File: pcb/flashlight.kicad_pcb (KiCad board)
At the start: 2 copper layers, 15.8 x 15.8 mm, 29 parts, among them IC1 TPS61200, IC2 PIC10F320

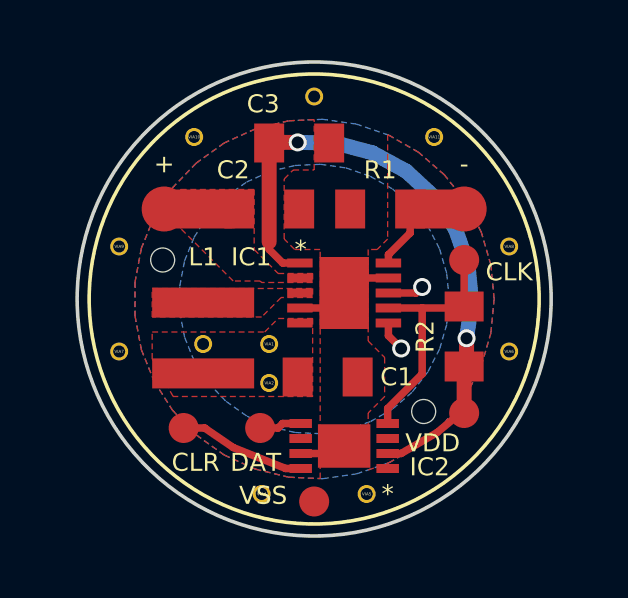
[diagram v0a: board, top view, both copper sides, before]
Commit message: move programming pads to bottom and add support extensions
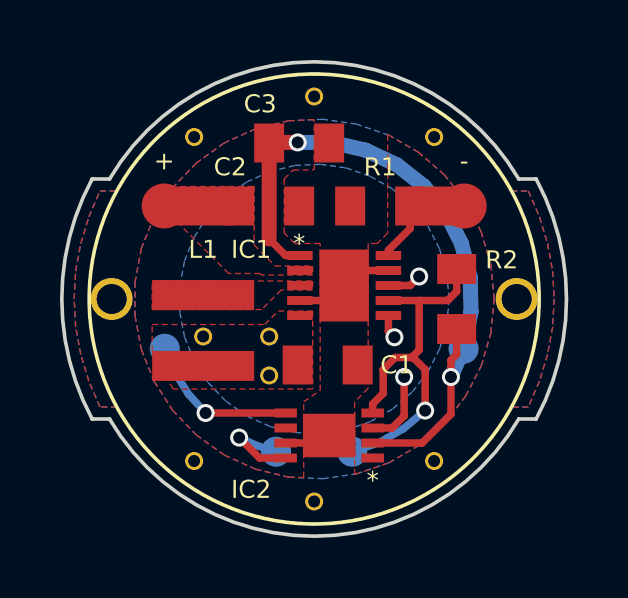
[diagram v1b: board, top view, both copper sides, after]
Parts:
- removed ? (x2): DRILL-0.8mm, modules:DRILL-0.8mm
- removed the VIA6 at (156.5, 101.8)
- removed the VIA7 at (143.5, 101.8)
- removed the VIA8 at (156.5, 98.2)
- removed VSS: VSS, modules:PAD-1.0mm
- added PIN1: PIN, modules:PIN-1.0mm, F.Cu at (143.2, 100.0)
- added PIN2: PIN, modules:PIN-1.0mm, F.Cu at (156.8, 100.0)
- MCLR: renamed from CLR; moved to B.Cu
- PCLK: renamed from CLK; moved to B.Cu
- PDAT: renamed from DAT; moved to B.Cu
- VDD: moved to B.Cu
- moved VIA6 13.4 mm to (154.0, 105.4)
- moved VIA9 11.1 mm to (154.0, 94.6)
- moved VIA7 8.00 mm to (146.0, 94.6)
- moved PCLK 7.40 mm to (151.3, 105.1)
- moved PDAT 4.13 mm to (145.0, 101.7)
- moved MCLR 3.18 mm to (148.7, 105.1)
- moved VIA4 2.50 mm to (146.0, 105.4)
- moved VDD 2.14 mm to (155.0, 101.7)
- moved VIA5 1.77 mm to (150.0, 106.8)
- moved R2 1.27 mm to (154.8, 100.0)
- moved IC2 0.61 mm to (150.5, 104.5)
- moved C1 0.40 mm to (150.4, 102.2)
- moved IC1 0.25 mm to (151.0, 99.5)
- moved L1 0.25 mm to (146.3, 101.0)
- moved VIA1 0.25 mm to (148.5, 101.2)
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- renumbered VIA10 to VIA6, VIA11 to VIA7, VIA12 to VIA8
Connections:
- IC2 pad 1: GND -> (no net)
- IC2 pad 3: (no net) -> SUPPLY
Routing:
- net N$4: track 8.45 -> 12.7 mm, vias 0 -> 1
- net N$6: track 1.41 -> 5.23 mm, vias 0 -> 1
- net SUPPLY: track 2.23 -> 4.47 mm, vias 2 -> 3
- net GND: track 4.92 -> 7.04 mm
- net N$3: track 21.2 -> 22.8 mm
- net N$7: track 4.24 -> 3.15 mm, vias 0 -> 1
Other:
- board size 15.8 x 15.8 mm -> 16.8 x 15.8 mm

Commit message: reduce radius of supply mask and move supply vias
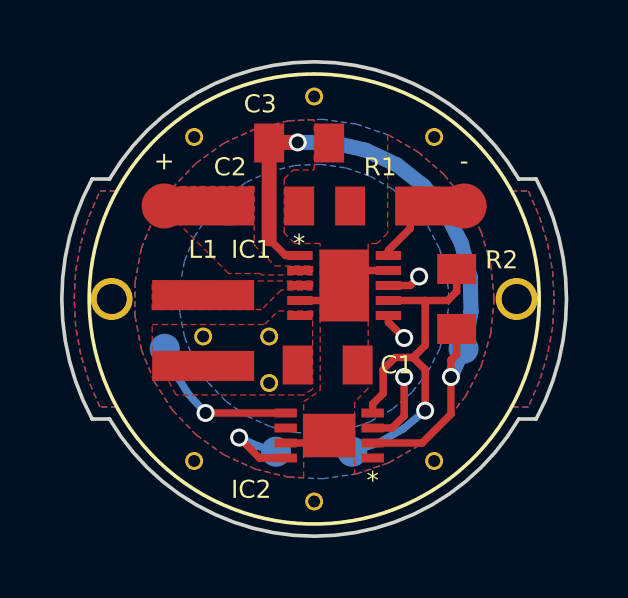
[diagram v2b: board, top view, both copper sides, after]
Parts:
- moved VIA2 0.25 mm to (148.5, 102.8)
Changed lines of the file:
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@@
     (thickness 1.6)
     (drawings 11)
-    (tracks 76)
+    (tracks 77)
     (zones 0)
     (modules 25)
@@
     (36 B.SilkS user)
     (37 F.SilkS user)
-    (38 B.Mask user hide)
+    (38 B.Mask user)
     (39 F.Mask user)
     (40 Dwgs.User user)
@@
   )
   (module modules:VIA-0.6mm (layer F.Cu)
-    (at 148.5 102.55)
+    (at 148.5 102.8)
     (fp_text reference VIA2 (at 0 0) (layer F.SilkS) hide
       (effects (font (size 0.2 0.2) (thickness 0.01)))
@@
   )
   (gr_circle (center 150 100) (end 157.5 100) (layer F.SilkS) (width 0.12))
-  (segment (start 152.475 100.55) (end 152.475 101.075) (width 0.25) (layer F.Cu) (net 1))
-  (segment (start 152.475 101.075) (end 152.675 101.275) (width 0.25) (layer F.Cu) (net 1))
-  (via (at 152.675 101.275) (size 0.6) (drill 0.4) (layers F.Cu B.Cu) (net 1))
+  (segment (start 152.475 100.55) (end 152.475 100.775) (width 0.25) (layer F.Cu) (net 1))
+  (via (at 153 101.3) (size 0.6) (drill 0.4) (layers F.Cu B.Cu) (net 1))
+  (segment (start 152.475 100.775) (end 153 101.3) (width 0.25) (layer F.Cu) (net 1))
   (segment (start 152.475 99.55) (end 153.2 99.55) (width 0.25) (layer F.Cu) (net 1))
   (via (at 153.5 99.25) (size 0.6) (drill 0.4) (layers F.Cu B.Cu) (net 1))
@@
   (via (at 154.56 102.6) (size 0.6) (drill 0.4) (layers F.Cu B.Cu) (net 3))
   (segment (start 147.25 96.9) (end 145 96.9) (width 1.3) (layer F.Cu) (net 5))
+  (segment (start 153.3 101.95) (end 153.7 101.55) (width 0.25) (layer F.Cu) (net 6))
+  (segment (start 153.7 101.55) (end 153.7 100.05) (width 0.25) (layer F.Cu) (net 6))
   (segment (start 153.7 102.35) (end 153.7 103.72) (width 0.25) (layer F.Cu) (net 6))
   (segment (start 151.27 105.09) (end 152.16 104.79) (width 0.25) (layer B.Cu) (net 6))
@@
   (segment (start 153.25 101.95) (end 153.3 101.95) (width 0.25) (layer F.Cu) (net 6))
   (segment (start 153.3 101.95) (end 153.7 102.35) (width 0.25) (layer F.Cu) (net 6))
-  (segment (start 153.25 101.95) (end 153.5 101.7) (width 0.25) (layer F.Cu) (net 6))
-  (segment (start 153.5 101.7) (end 153.5 100.05) (width 0.25) (layer F.Cu) (net 6))
   (segment (start 154.75 99) (end 154.75 99.75) (width 0.25) (layer F.Cu) (net 6))
   (segment (start 154.75 99.75) (end 154.45 100.05) (width 0.25) (layer F.Cu) (net 6))
-  (segment (start 154.45 100.05) (end 153.5 100.05) (width 0.25) (layer F.Cu) (net 6))
+  (segment (start 154.45 100.05) (end 153.7 100.05) (width 0.25) (layer F.Cu) (net 6))
+  (segment (start 153.7 100.05) (end 153.5 100.05) (width 0.25) (layer F.Cu) (net 6))
   (segment (start 153.5 100.05) (end 152.475 100.05) (width 0.25) (layer F.Cu) (net 6))
   (segment (start 151.95 103.8) (end 151.95 103.5) (width 0.25) (layer F.Cu) (net 6))
@@
     (polygon
       (pts
-        (xy 153.5 100) (xy 153.44 100.66) (xy 153.25 101.3) (xy 152.94 101.89) (xy 152.53 102.42)
-        (xy 152.03 102.85) (xy 151.45 103.18) (xy 150.83 103.4) (xy 150.17 103.5) (xy 149.5 103.46)
-        (xy 148.86 103.31) (xy 148.25 103.03) (xy 147.71 102.65) (xy 147.25 102.16) (xy 146.89 101.6)
-        (xy 146.64 100.99) (xy 146.52 100.33) (xy 146.52 99.67) (xy 146.64 99.01) (xy 146.89 98.4)
-        (xy 147.25 97.84) (xy 147.71 97.35) (xy 148.25 96.97) (xy 148.86 96.69) (xy 149.5 96.54)
-        (xy 150.17 96.5) (xy 150.83 96.6) (xy 151.45 96.82) (xy 152.03 97.15) (xy 152.53 97.58)
-        (xy 152.94 98.11) (xy 153.25 98.7) (xy 153.44 99.34)
+        (xy 153 100) (xy 152.95 100.57) (xy 152.79 101.11) (xy 152.52 101.62) (xy 152.17 102.07)
+        (xy 151.74 102.44) (xy 151.25 102.73) (xy 150.71 102.92) (xy 150.14 103) (xy 149.57 102.97)
+        (xy 149.02 102.84) (xy 148.5 102.6) (xy 148.04 102.27) (xy 147.64 101.85) (xy 147.33 101.37)
+        (xy 147.12 100.85) (xy 147.01 100.29) (xy 147.01 99.71) (xy 147.12 99.15) (xy 147.33 98.63)
+        (xy 147.64 98.15) (xy 148.04 97.73) (xy 148.5 97.4) (xy 149.02 97.16) (xy 149.57 97.03)
+        (xy 150.14 97) (xy 150.71 97.08) (xy 151.25 97.27) (xy 151.74 97.56) (xy 152.17 97.93)
+        (xy 152.52 98.38) (xy 152.79 98.89) (xy 152.95 99.43)
       )
     )
@@
     (polygon
       (pts
-        (xy 149.95 103) (xy 145.3 103) (xy 144.6 101.75) (xy 144.6 100.85) (xy 148.35 100.85)
-        (xy 148.8 100.4) (xy 149.95 100.4)
+        (xy 149.95 103) (xy 149.65 103.2) (xy 145.4 103.2) (xy 144.6 101.75) (xy 144.6 100.85)
+        (xy 148.35 100.85) (xy 148.8 100.4) (xy 149.95 100.4)
       )
     )
